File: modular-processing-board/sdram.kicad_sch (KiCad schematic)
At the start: 20 parts, among them U301 W9825G6KH-6, U302 W9825G6KH-6

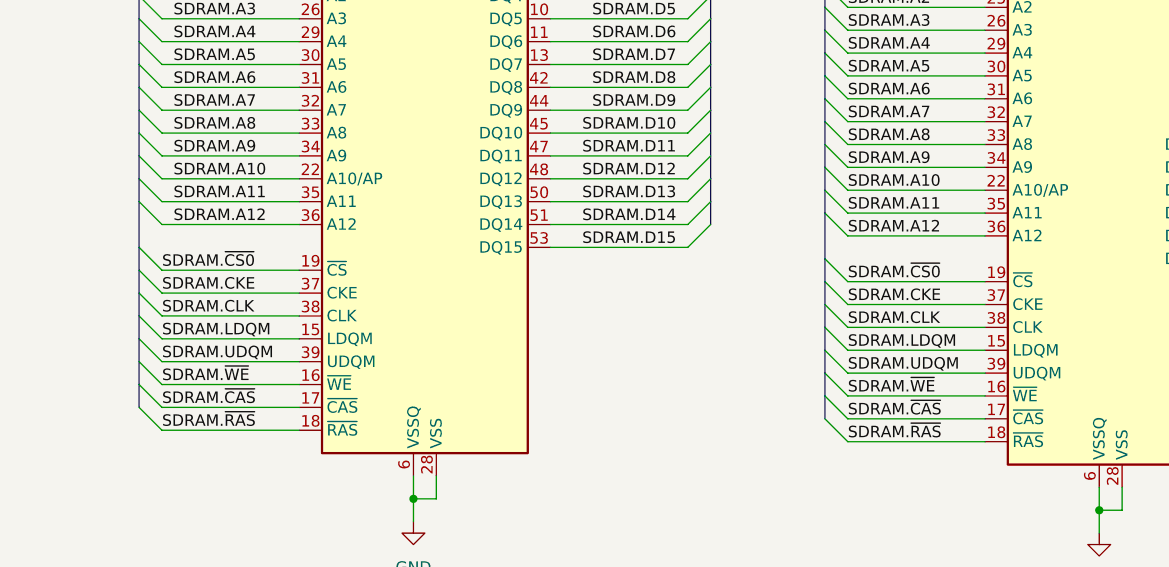
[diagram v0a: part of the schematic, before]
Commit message: basicsic pinout/component selection done, added SDRAM pins (next) Add parallel pins, add connections to pinheaders
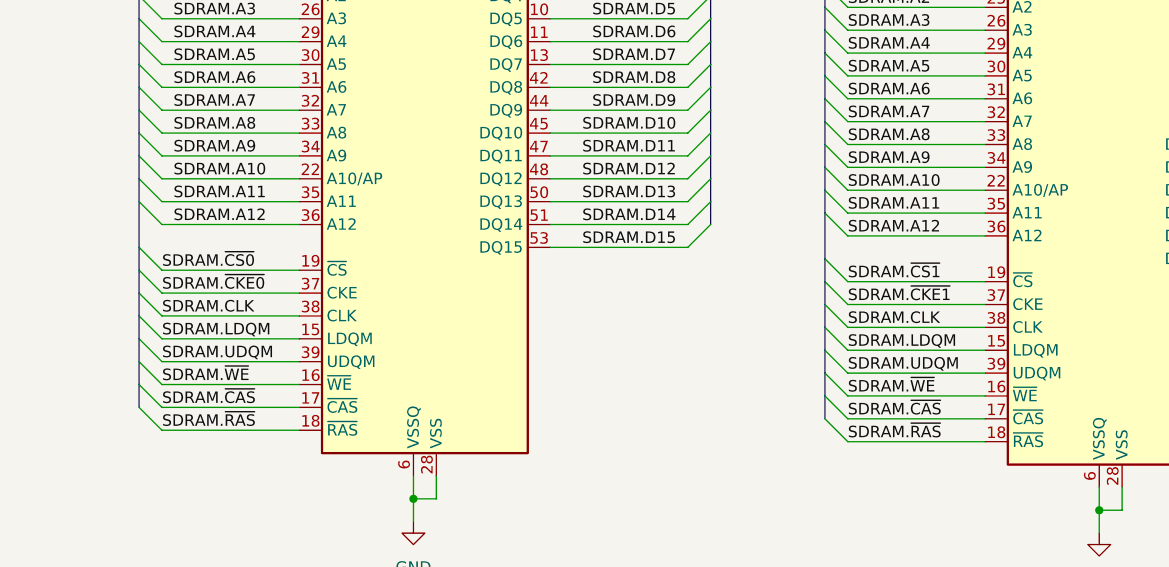
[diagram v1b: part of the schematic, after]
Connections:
- net SDRAM.~{CS0}: no longer U302.19 (~{CS})
- net SDRAM.CKE renamed SDRAM.~{CKE0}
- net SDRAM.~{CKE0}: no longer U302.37 (CKE)
- new net SDRAM.~{CKE1}: U302.37 (CKE)
- new net SDRAM.~{CS1}: U302.19 (~{CS})
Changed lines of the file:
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@@
 	)
 	(bus_alias "SDRAM_CTL"
-		(members "A[12..0]" "~{CS[0..1]}" "CKE" "CLK" "LDQM" "UDQM" "~{WE}" "~{CAS}"
-			"~{RAS}" "BS[0..1]" "CLK"
+		(members "A[12..0]" "~{CS[0..1]}" "~{CKE[0..1]}" "CLK" "LDQM" "UDQM" "~{WE}"
+			"~{CAS}" "~{RAS}" "BS[0..1]" "CLK"
 		)
 	)
@@
 		)
 	)
-	(label "SDRAM.CKE"
+	(label "SDRAM.~{CKE0}"
 		(at 127 93.98 0)
 		(effects
@@
 		)
 	)
-	(label "SDRAM.~{CS0}"
+	(label "SDRAM.~{CS1}"
 		(at 203.2 92.71 0)
 		(effects
@@
 		)
 	)
-	(label "SDRAM.CKE"
+	(label "SDRAM.~{CKE1}"
 		(at 203.2 95.25 0)
 		(effects

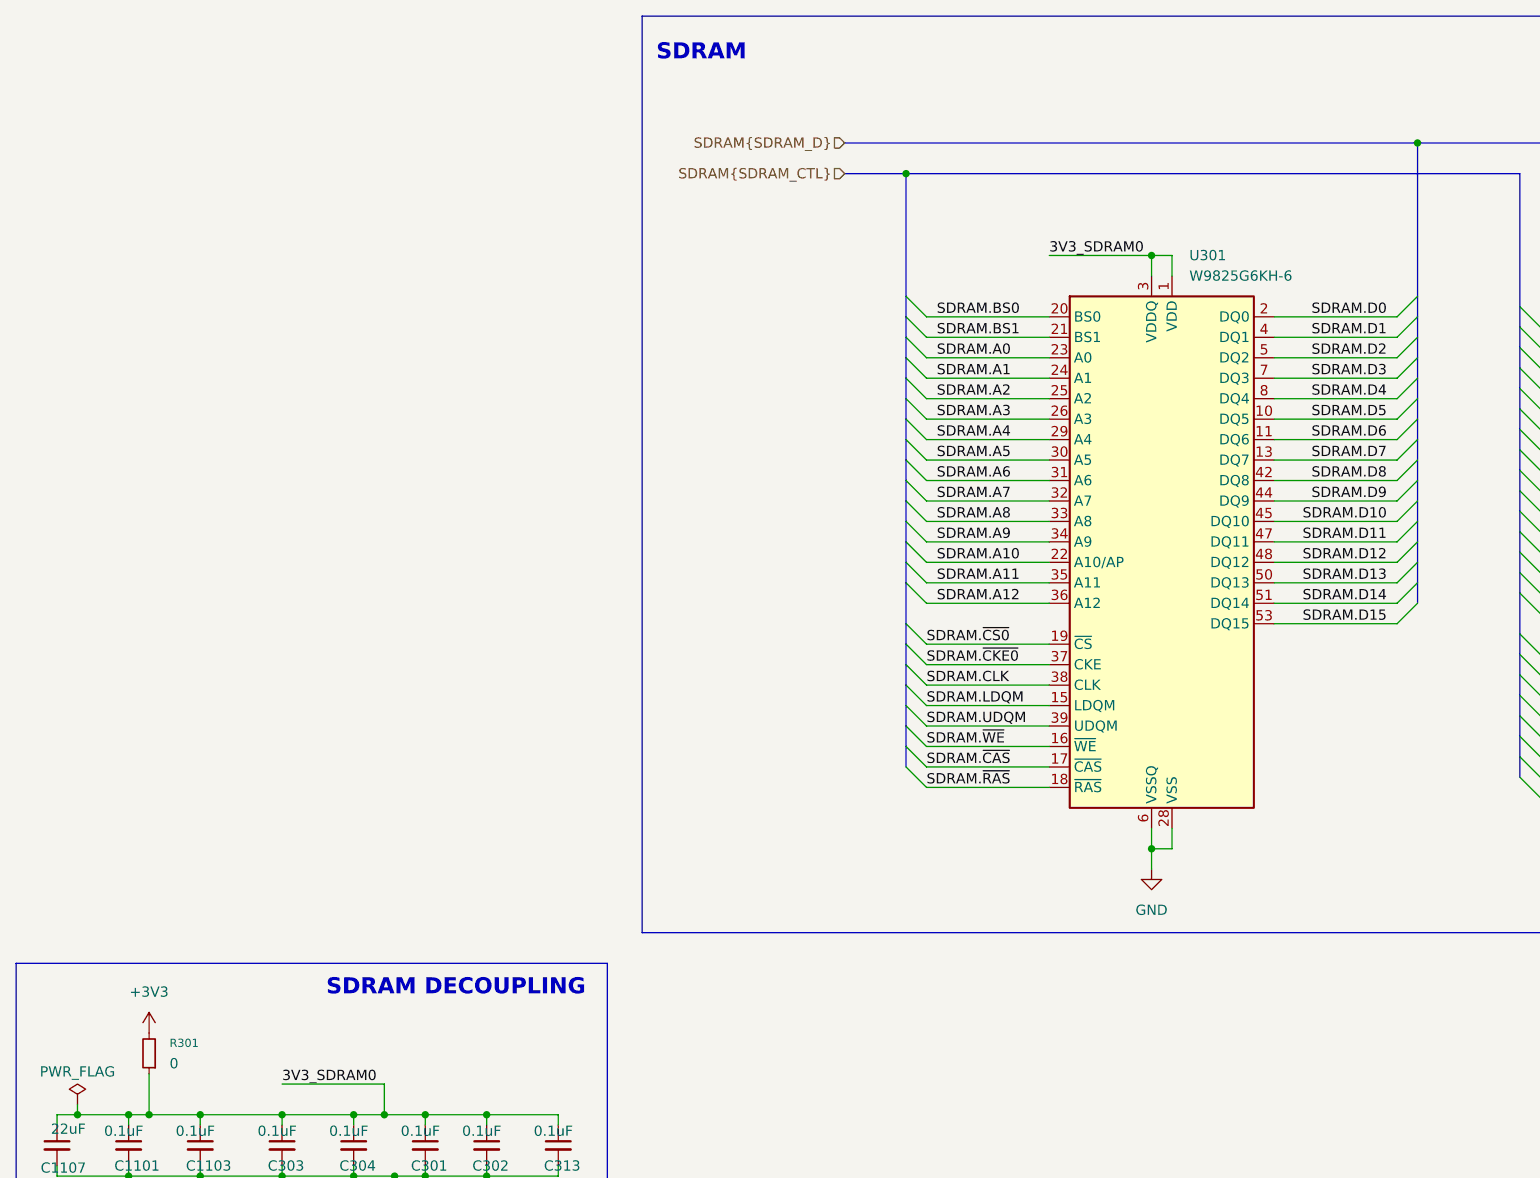
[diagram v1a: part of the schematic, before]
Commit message: added parallel slave bus, SWO, USB (next) add small PSU for CPU-board, add ethernet PHY, add correct USB connector
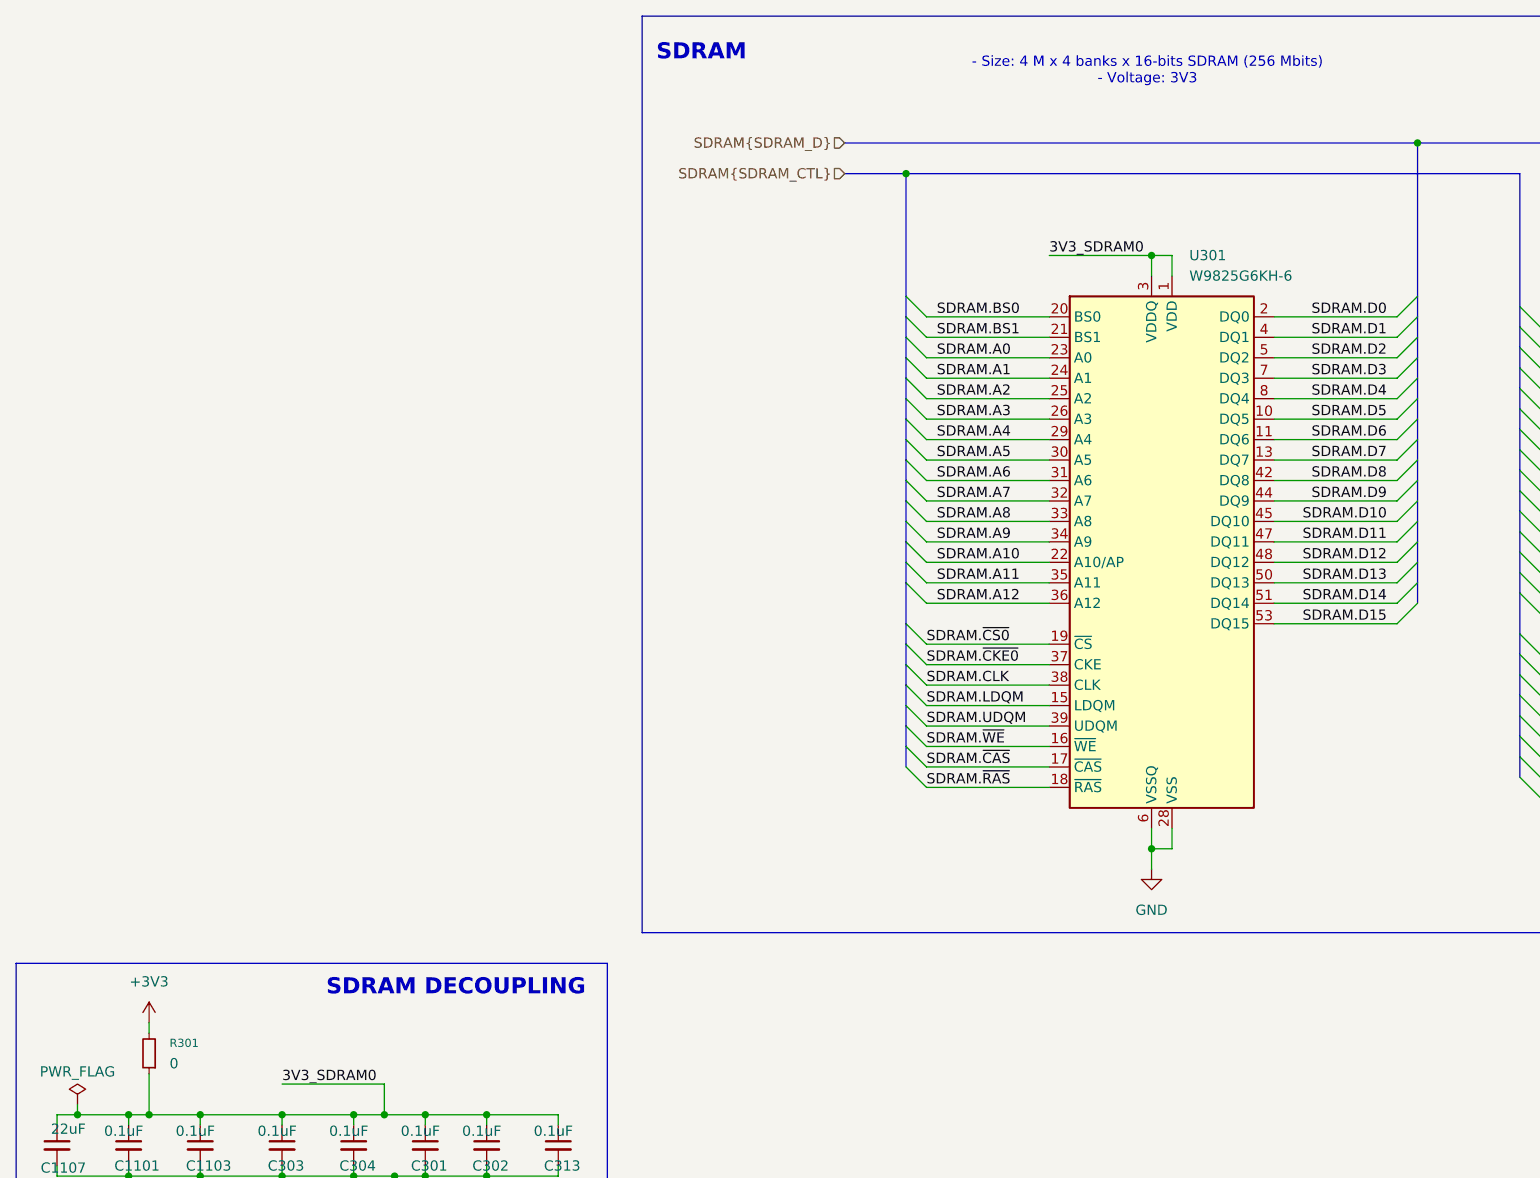
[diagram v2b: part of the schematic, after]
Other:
- note added: "- Size: 4 M x 4 banks x 16-bits SDRAM (256 Mbits) - Voltage: 3V3"
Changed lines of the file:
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@@
 		(members "IO[1..12]")
 	)
+	(bus_alias "PSSI"
+		(members "PDCK" "D[0..15]" "DE" "RDY")
+	)
 	(bus_alias "RGMII_MDIO"
 		(members "DATA" "CLK")
@@
 	(bus_alias "SDRAM_CTL"
 		(members "A[12..0]" "~{CS[0..1]}" "~{CKE[0..1]}" "CLK" "LDQM" "UDQM" "~{WE}"
-			"~{CAS}" "~{RAS}" "BS[0..1]" "CLK"
+			"~{CAS}" "~{RAS}" "BS[0..1]"
 		)
 	)
@@
 		(members "IO[0..12]")
 	)
-	(bus_alias "USB_ULPI"
-		(members "CLK" "D[0..7]" "RST" "STP" "DIR" "NXT")
-	)
 	(rectangle
 		(start 13.97 131.064)
@@
 		)
 	)
+	(text "- Size: 4 M x 4 banks x 16-bits SDRAM (256 Mbits)\n- Voltage: 3V3"
+		(exclude_from_sim no)
+		(at 154.432 20.32 0)
+		(effects
+			(font
+				(size 1.27 1.27)
+			)
+		)
+	)
 	(junction
 		(at 58.42 177.8)
@@
 	(wire
 		(pts
+			(xy 30.48 138.43) (xy 30.48 139.7)
+		)
+		(stroke
+			(width 0)
+			(type default)
+		)
+	)
+	(wire
+		(pts
 			(xy 170.18 73.66) (xy 185.42 73.66)
 		)
@@
 		)
 	)
-	(hierarchical_label "SDRAM{SDRAM_CTL}"
+	(hierarchical_label "SDRAM{SDRAM_D}"
 		(shape input)
-		(at 116.84 33.02 180)
+		(at 116.84 29.21 180)
 		(effects
 			(font
@@
 		)
 	)
-	(hierarchical_label "SDRAM{SDRAM_D}"
+	(hierarchical_label "SDRAM{SDRAM_CTL}"
 		(shape input)
-		(at 116.84 29.21 180)
+		(at 116.84 33.02 180)
 		(effects
 			(font
@@
 	(symbol
 		(lib_id "power:+3V3")
-		(at 30.48 139.7 0)
+		(at 30.48 138.43 0)
 		(unit 1)
 		(exclude_from_sim no)
@@
 		(fields_autoplaced yes)
 		(property "Reference" "#PWR0303"
-			(at 30.48 143.51 0)
+			(at 30.48 142.24 0)
 			(effects
 				(font
@@
 		)
 		(property "Value" "+3V3"
-			(at 30.48 134.62 0)
+			(at 30.48 133.35 0)
 			(effects
 				(font
@@
 		)
 		(property "Footprint" ""
-			(at 30.48 139.7 0)
+			(at 30.48 138.43 0)
 			(effects
 				(font
@@
 		)
 		(property "Datasheet" ""
-			(at 30.48 139.7 0)
+			(at 30.48 138.43 0)
 			(effects
 				(font
@@
 		)
 		(property "Description" "Power symbol creates a global label with name \"+3V3\""
-			(at 30.48 139.7 0)
+			(at 30.48 138.43 0)
 			(effects
 				(font

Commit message: completed schematic
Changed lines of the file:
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@@
 	)
 	(junction
-		(at 124.46 33.02)
-		(diameter 0)
-		(color 0 0 0 0)
-	)
-	(junction
 		(at 46.99 149.86)
 		(diameter 0)
@@
 		)
 	)
-	(wire
-		(pts
-			(xy 127 91.44) (xy 142.24 91.44)
-		)
-		(stroke
-			(width 0)
-			(type default)
-		)
-	)
 	(bus
 		(pts
@@
 		)
 	)
+	(wire
+		(pts
+			(xy 127 91.44) (xy 142.24 91.44)
+		)
+		(stroke
+			(width 0)
+			(type default)
+		)
+	)
 	(bus
 		(pts
@@
 	(bus
 		(pts
+			(xy 200.66 34.29) (xy 200.66 49.53)
+		)
+		(stroke
+			(width 0)
+			(type default)
+		)
+	)
+	(bus
+		(pts
 			(xy 200.66 95.25) (xy 200.66 97.79)
 		)
@@
 	(bus
 		(pts
-			(xy 200.66 33.02) (xy 200.66 49.53)
-		)
-		(stroke
-			(width 0)
-			(type default)
-		)
-	)
-	(bus
-		(pts
 			(xy 124.46 73.66) (xy 124.46 76.2)
 		)
@@
 	(bus
 		(pts
-			(xy 124.46 33.02) (xy 200.66 33.02)
+			(xy 207.01 34.29) (xy 200.66 34.29)
 		)
 		(stroke
@@
 		)
 	)
+	(label "SDRAM.~{CS0}"
+		(at 127 91.44 0)
+		(effects
+			(font
+				(size 1.27 1.27)
+			)
+			(justify left bottom)
+		)
+	)
 	(label "SDRAM.D12"
 		(at 184.15 81.28 180)
@@
 		)
 	)
-	(label "SDRAM.~{CS0}"
-		(at 127 91.44 0)
-		(effects
-			(font
-				(size 1.27 1.27)
-			)
-			(justify left bottom)
-		)
-	)
 	(label "SDRAM.BS1"
 		(at 128.27 53.34 0)
@@
 		)
 	)
+	(hierarchical_label "SDRAM{SDRAM_CTL}"
+		(shape input)
+		(at 207.01 34.29 0)
+		(effects
+			(font
+				(size 1.27 1.27)
+			)
+			(justify left)
+		)
+	)

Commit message: various changes to schematic (next) add bias resistors after testing results on acoustic-carrier-board
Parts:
- C1101, C1103, C301, C302, C303, C304, C305, C306, C307, C308, C309, C310, C311, C313: footprint Capacitor_SMD:C_0201_0603Metric -> Capacitor_SMD:C_0402_1005Metric; LPN (none) -> C307331; MPN (none) -> CL05B104KB54PNC

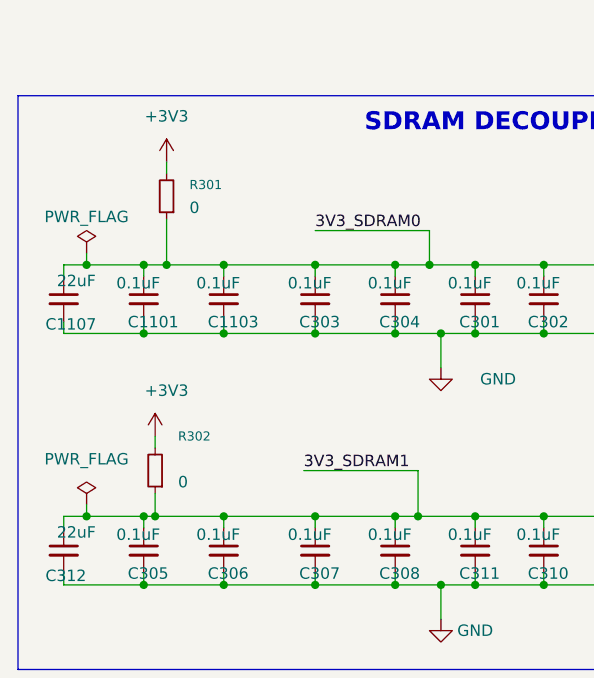
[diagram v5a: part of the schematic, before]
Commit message: removed power input jumpers to single one, added trace impedances and production restrictions (next) route sdram
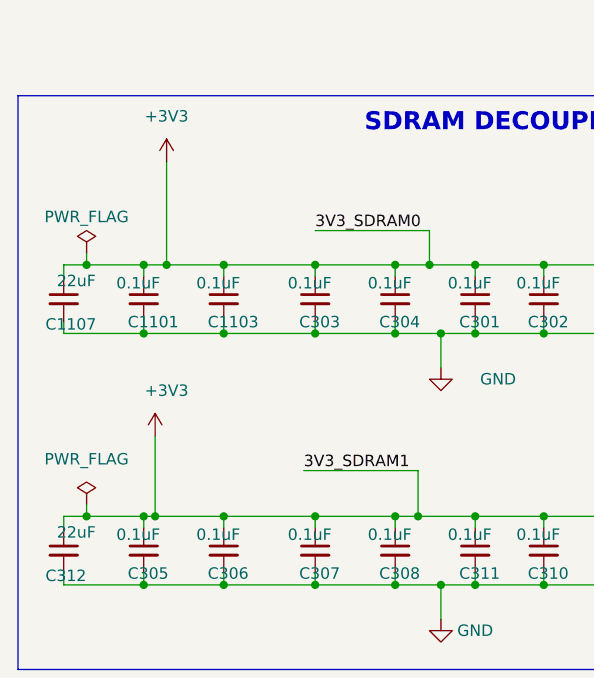
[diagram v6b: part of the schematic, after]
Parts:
- removed R301, R302: 0, Resistor_SMD:R_0805_2012Metric_Pad1.20x1.40mm_HandSolder, symbol Device:R_Small
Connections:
- net 3V3_SDRAM0 is gone; now on net +3V3: C1101.1, C1103.1, C1107.1, C301.1, C302.1, C303.1, C304.1, C313.1, U301.1 (VDD), U301.14 (VDD), U301.27 (VDD), U301.3 (VDDQ), U301.43 (VDDQ), U301.49 (VDDQ), U301.9 (VDDQ)
- net 3V3_SDRAM1 is gone; now on net +3V3: C305.1, C306.1, C307.1, C308.1, C309.1, C310.1, C311.1, C312.1, U302.1 (VDD), U302.14 (VDD), U302.27 (VDD), U302.3 (VDDQ), U302.43 (VDDQ), U302.49 (VDDQ), U302.9 (VDDQ)
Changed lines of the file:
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@@
 	(wire
 		(pts
+			(xy 30.48 138.43) (xy 30.48 149.86)
+		)
+		(stroke
+			(width 0)
+			(type default)
+		)
+	)
+	(wire
+		(pts
 			(xy 127 96.52) (xy 142.24 96.52)
 		)
@@
 	(wire
 		(pts
-			(xy 30.48 144.78) (xy 30.48 149.86)
-		)
-		(stroke
-			(width 0)
-			(type default)
-		)
-	)
-	(wire
-		(pts
 			(xy 72.39 177.8) (xy 81.28 177.8)
 		)
@@
 		)
 	)
-	(wire
-		(pts
-			(xy 29.21 175.26) (xy 29.21 177.8)
-		)
-		(stroke
-			(width 0)
-			(type default)
-		)
-	)
 	(bus
 		(pts
@@
 	(wire
 		(pts
-			(xy 30.48 138.43) (xy 30.48 139.7)
-		)
-		(stroke
-			(width 0)
-			(type default)
-		)
-	)
-	(wire
-		(pts
 			(xy 170.18 73.66) (xy 185.42 73.66)
 		)
@@
 	(wire
 		(pts
-			(xy 29.21 168.91) (xy 29.21 170.18)
+			(xy 29.21 168.91) (xy 29.21 177.8)
 		)
 		(stroke
@@
 	)
 	(symbol
-		(lib_id "Device:R_Small")
-		(at 29.21 172.72 180)
-		(unit 1)
-		(exclude_from_sim no)
-		(in_bom yes)
-		(on_board yes)
-		(dnp no)
-		(property "Reference" "R302"
-			(at 31.75 168.9099 0)
-			(effects
-				(font
-					(size 1.016 1.016)
-				)
-				(justify right)
-			)
-		)
-		(property "Value" "0"
-			(at 31.75 173.9899 0)
-			(effects
-				(font
-					(size 1.27 1.27)
-				)
-				(justify right)
-			)
-		)
-		(property "Footprint" "Resistor_SMD:R_0805_2012Metric_Pad1.20x1.40mm_HandSolder"
-			(at 29.21 172.72 0)
-			(effects
-				(font
-					(size 1.27 1.27)
-				)
-				(hide yes)
-			)
-		)
-		(property "Datasheet" "https://jlcpcb.com/api/file/downloadByFileSystemAccessId/8579706711113842688"
-			(at 29.21 172.72 0)
-			(effects
-				(font
-					(size 1.27 1.27)
-				)
-				(hide yes)
-			)
-		)
-		(property "Description" "125mW"
-			(at 29.21 172.72 0)
-			(effects
-				(font
-					(size 1.27 1.27)
-				)
-				(hide yes)
-			)
-		)
-		(property "Availability" ""
-			(at 29.21 172.72 90)
-			(effects
-				(font
-					(size 1.27 1.27)
-				)
-				(hide yes)
-			)
-		)
-		(property "LCSC Part Number" "C17477"
-			(at 29.21 172.72 90)
-			(effects
-				(font
-					(size 1.27 1.27)
-				)
-				(hide yes)
-			)
-		)
-		(property "Manufacturing Part Number" "0805W8F0000T5E"
-			(at 29.21 172.72 90)
-			(effects
-				(font
-					(size 1.27 1.27)
-				)
-				(hide yes)
-			)
-		)
-		(pin "2"
-		)
-		(pin "1"
-		)
-		(instances
-			(project "modular-processing-board"
-				(path "/73b5a92f-908b-4f97-a96c-14ee20a7f293/af776c85-f6b4-42a5-8874-b51ab1bab382"
-					(reference "R302")
-					(unit 1)
-				)
-			)
-		)
-	)
-	(symbol
 		(lib_id "Device:C_Small")
 		(at 46.99 181.61 0)
@@
 					(unit 1)
 				)
-			)
-		)
-	)
-	(symbol
-		(lib_id "Device:R_Small")
-		(at 30.48 142.24 180)
-		(unit 1)
-		(exclude_from_sim no)
-		(in_bom yes)
-		(on_board yes)
-		(dnp no)
-		(fields_autoplaced yes)
-		(property "Reference" "R301"
-			(at 33.02 140.9699 0)
-			(effects
-				(font
-					(size 1.016 1.016)
-				)
-				(justify right)
-			)
-		)
-		(property "Value" "0"
-			(at 33.02 143.5099 0)
-			(effects
-				(font
-					(size 1.27 1.27)
-				)
-				(justify right)
-			)
-		)
-		(property "Footprint" "Resistor_SMD:R_0805_2012Metric_Pad1.20x1.40mm_HandSolder"
-			(at 30.48 142.24 0)
-			(effects
-				(font
-					(size 1.27 1.27)
-				)
-				(hide yes)
-			)
-		)
-		(property "Datasheet" "https://jlcpcb.com/api/file/downloadByFileSystemAccessId/8579706711113842688"
-			(at 30.48 142.24 0)
-			(effects
-				(font
-					(size 1.27 1.27)
-				)
-				(hide yes)
-			)
-		)
-		(property "Description" "125mW"
-			(at 30.48 142.24 0)
-			(effects
-				(font
-					(size 1.27 1.27)
-				)
-				(hide yes)
-			)
-		)
-		(property "Availability" ""
-			(at 30.48 142.24 90)
-			(effects
-				(font
-					(size 1.27 1.27)
-				)
-				(hide yes)
-			)
-		)
-		(property "LCSC Part Number" "C17477"
-			(at 30.48 142.24 90)
-			(effects
-				(font
-					(size 1.27 1.27)
-				)
-				(hide yes)
-			)
-		)
-		(property "Manufacturing Part Number" "0805W8F0000T5E"
-			(at 30.48 142.24 90)
-			(effects
-				(font
-					(size 1.27 1.27)
-				)
-				(hide yes)
-			)
-		)
-		(pin "2"
-		)
-		(pin "1"
-		)
-		(instances
-			(project "modular-processing-board"
-				(path "/73b5a92f-908b-4f97-a96c-14ee20a7f293/af776c85-f6b4-42a5-8874-b51ab1bab382"
-					(reference "R301")
-					(unit 1)
-				)

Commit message: figuring out delay matching for sdram
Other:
- note added: "SDRAM PHY Rise / Fall / Setup / Hold times: - 1 ns - t_setup-time: 1.5 ns - t_hold-time: 1 ns MCU Rise / Fall / Setup / Hold times -"
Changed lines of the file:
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@@
 		)
 	)
+	(text "SDRAM PHY Rise / Fall / Setup / Hold times:\n- 1 ns\n- t_setup-time: 1.5 ns\n- t_hold-time: 1 ns\nMCU Rise / Fall / Setup / Hold times\n- "
+		(exclude_from_sim no)
+		(at 93.472 121.412 0)
+		(effects
+			(font
+				(size 1.27 1.27)
+			)
+			(justify left)
+		)
+	)
 	(text "SDRAM DECOUPLING"
 		(exclude_from_sim no)
@@
 		(on_board yes)
 		(dnp no)
-		(fields_autoplaced yes)
 		(property "Reference" "#PWR0301"
 			(at 154.94 125.73 0)
@@
 		)
 		(property "Value" "GND"
-			(at 154.94 124.46 0)
+			(at 157.48 119.38 0)
 			(effects
 				(font
@@
 		(on_board yes)
 		(dnp no)
-		(fields_autoplaced yes)
 		(property "Reference" "#PWR0302"
 			(at 231.14 127 0)
@@
 		)
 		(property "Value" "GND"
-			(at 231.14 125.73 0)
+			(at 233.934 120.904 0)
 			(effects
 				(font
